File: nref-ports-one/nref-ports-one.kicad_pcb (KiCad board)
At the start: 2 copper layers, 84.9 x 17.5 mm, 4 parts, among them J3 USB_C_Receptacle

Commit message: ports-one WIP
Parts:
- removed REF**: WURTH_692121230100, footprints:WURTH_692121230100
- added C1: 1nF, Capacitor_SMD:C_0603_1608Metric, F.Cu at (137.7, 98.8)
- added C10: 0.1uF, Capacitor_SMD:C_0402_1005Metric, F.Cu at (103.6, 145.8)
- added C11: 10uF, Capacitor_SMD:C_0603_1608Metric, F.Cu at (102.2, 147.3)
- added C12: 10uF, Capacitor_SMD:C_0603_1608Metric, F.Cu at (102.2, 149.9)
- added C13: 0.1uF, Capacitor_SMD:C_0402_1005Metric, F.Cu at (111.6, 125.3)
- added C14: 0.1uF, Capacitor_SMD:C_0402_1005Metric, F.Cu at (109.1, 120.2)
- added C15: 0.1uF, Capacitor_SMD:C_0402_1005Metric, F.Cu at (109.1, 122.2)
- added C16: 10uF, Capacitor_SMD:C_0603_1608Metric, F.Cu at (106.2, 150.9)
- added C17: 47uF, Capacitor_SMD:C_1206_3216Metric, F.Cu at (118.6, 112.5)
- added C18: 0.1uF, Capacitor_SMD:C_0402_1005Metric, F.Cu at (117.1, 116.7)
- added C19: 22uF, Capacitor_SMD:C_0805_2012Metric, F.Cu at (104.1, 136.8)
- added C2: 0.1uF, Capacitor_SMD:C_0402_1005Metric, F.Cu at (137.7, 104.8)
- added C20: 22uF, Capacitor_SMD:C_0805_2012Metric, F.Cu at (104.2, 134.1)
- added C21: 47uF, Capacitor_SMD:C_1206_3216Metric, F.Cu at (118.5, 107.0)
- added C22: DNP, Capacitor_SMD:C_0402_1005Metric, F.Cu at (95.6, 149.1)
- added C23: 0.1uF, Capacitor_SMD:C_0402_1005Metric, F.Cu at (91.6, 127.1)
- added C24: 0.1uF, Capacitor_SMD:C_0402_1005Metric, F.Cu at (94.4, 115.3)
- added C25: 470nF, Capacitor_SMD:C_0603_1608Metric, F.Cu at (93.7, 122.9)
- added C26: 0.1uF, Capacitor_SMD:C_0402_1005Metric, F.Cu at (136.4, 123.3)
- added C27: 0.1uF, Capacitor_SMD:C_0402_1005Metric, F.Cu at (138.4, 121.2)
- added C28: 0.1uF, Capacitor_SMD:C_0402_1005Metric, F.Cu at (138.4, 123.2)
- added C29: 0.1uF, Capacitor_SMD:C_0402_1005Metric, F.Cu at (138.4, 125.2)
- added C3: 0.1uF, Capacitor_SMD:C_0402_1005Metric, F.Cu at (137.7, 106.8)
- added C30: 10uF, Capacitor_SMD:C_0603_1608Metric, F.Cu at (110.2, 140.8)
- added C31: 0.1uF, Capacitor_SMD:C_0402_1005Metric, F.Cu at (139.9, 123.1)
- added C32: 0.1uF, Capacitor_SMD:C_0402_1005Metric, F.Cu at (185.4, 128.1)
- added C33: 0.1uF, Capacitor_SMD:C_0402_1005Metric, F.Cu at (173.8, 112.2)
- added C34: 0.1uF, Capacitor_SMD:C_0402_1005Metric, F.Cu at (175.8, 112.2)
- added C35: 0.1uF, Capacitor_SMD:C_0402_1005Metric, F.Cu at (177.7, 112.2)
- added C36: 0.1uF, Capacitor_SMD:C_0402_1005Metric, F.Cu at (179.7, 112.2)
- added C37: 0.1uF, Capacitor_SMD:C_0402_1005Metric, F.Cu at (189.3, 135.7)
- added C4: 0.1uF, Capacitor_SMD:C_0402_1005Metric, F.Cu at (137.7, 108.7)
- added C5: 0.1uF, Capacitor_SMD:C_0402_1005Metric, F.Cu at (137.7, 110.7)
- added C6: 10uF, Capacitor_SMD:C_0603_1608Metric, F.Cu at (106.2, 143.3)
- added C7: 0.1uF, Capacitor_SMD:C_0402_1005Metric, F.Cu at (99.7, 131.7)
- added C8: 0.1uF, Capacitor_SMD:C_0402_1005Metric, F.Cu at (119.7, 117.6)
- added C9: 0.1uF, Capacitor_SMD:C_0402_1005Metric, F.Cu at (97.7, 134.6)
- added D1: LED_Small, LED_SMD:LED_0603_1608Metric, F.Cu at (167.2, 103.4)
- added D2: LED_Small, LED_SMD:LED_0603_1608Metric, F.Cu at (169.3, 103.4)
- added D3: SS54, Diode_SMD:D_SMA, F.Cu at (184.6, 138.7)
- added D4: PMEG4050EP,115, Diode_SMD:D_SOD-128, F.Cu at (183.6, 144.3)
- added FB1: 100@100MHz 3A, Inductor_SMD:L_0603_1608Metric, F.Cu at (96.2, 144.3)
- added FB10: 100@100MHz 3A, Inductor_SMD:L_0603_1608Metric, F.Cu at (122.9, 122.8)
- added FB2: DNP, Inductor_SMD:L_0603_1608Metric, F.Cu at (110.2, 145.8)
- added FB3: 100@100MHz 3A, Inductor_SMD:L_0603_1608Metric, F.Cu at (110.2, 148.4)
- added FB4: 100@100MHz 3A, Inductor_SMD:L_0603_1608Metric, F.Cu at (110.2, 150.9)
- added FB5: 100@100MHz 3A, Inductor_SMD:L_0603_1608Metric, F.Cu at (96.2, 146.4)
- added FB6: 100@100MHz 3A, Inductor_SMD:L_0603_1608Metric, F.Cu at (97.2, 140.3)
- added FB7: 100@100MHz 3A, Inductor_SMD:L_0603_1608Metric, F.Cu at (118.2, 123.3)
- added FB8: 100@100MHz 3A, Inductor_SMD:L_0603_1608Metric, F.Cu at (106.8, 128.7)
- added FB9: 100@100MHz 3A, Inductor_SMD:L_0603_1608Metric, F.Cu at (102.3, 125.1)
- added J1: CONN_HEAD, footprints:CUI_SJ-43614-SMT, F.Cu at (111.8, 108.0)
- added J10: CONN_SPK, Connector_Molex:Molex_PicoBlade_53261-0271_1x02-1MP_P1.25mm_Horizontal, F.Cu at (104.0, 117.0)
- added J2: DM3AT-SF-PEJM5, Connector_Card:microSD_HC_Hirose_DM3AT-SF-PEJM5, F.Cu at (129.2, 110.3)
- added J3: 09452812561, footprints:09452812561, F.Cu at (159.3, 110.2)
- added J5: Conn_01x10_Pin, Connector_FFC-FPC:Hirose_FH12-10S-0.5SH_1x10-1MP_P0.50mm_Horizontal, F.Cu at (117.7, 131.1)
- added J6: Conn_01x14_Pin, Connector_FFC-FPC:Hirose_FH12-14S-0.5SH_1x14-1MP_P0.50mm_Horizontal, F.Cu at (142.0, 131.0)
- added J7: Conn_01x12_Pin, Connector_FFC-FPC:Hirose_FH12-12S-0.5SH_1x12-1MP_P0.50mm_Horizontal, F.Cu at (154.8, 131.0)
- added J8: PWR, Connector_JST:JST_SH_SM09B-SRSS-TB_1x09-1MP_P1.00mm_Horizontal, F.Cu at (176.6, 129.9)
- added J9: Conn_01x10_Pin, Connector_FFC-FPC:Hirose_FH12-10S-0.5SH_1x10-1MP_P0.50mm_Horizontal, F.Cu at (129.6, 131.0)
- added L1: 15uH, Inductor_SMD:L_Taiyo-Yuden_NR-30xx, F.Cu at (102.3, 122.1)
- added L2: 15uH, Inductor_SMD:L_Taiyo-Yuden_NR-30xx, F.Cu at (106.9, 125.6)
- added R1: 1k, Resistor_SMD:R_0402_1005Metric, F.Cu at (167.0, 105.8)
- added R10: 33, Resistor_SMD:R_0402_1005Metric, F.Cu at (116.2, 126.9)
- added R11: 33, Resistor_SMD:R_0402_1005Metric, F.Cu at (115.2, 126.9)
- added R12: 100k, Resistor_SMD:R_0402_1005Metric, F.Cu at (107.1, 133.5)
- added R13: 2.2k, Resistor_SMD:R_0402_1005Metric, F.Cu at (108.1, 137.0)
- added R14: 10k, Resistor_SMD:R_0402_1005Metric, F.Cu at (133.5, 126.6)
- added R15: 0, Resistor_SMD:R_0402_1005Metric, F.Cu at (134.0, 124.5)
- added R16: 100k, Resistor_SMD:R_0402_1005Metric, F.Cu at (121.0, 127.0)
- added R17: 0, Resistor_SMD:R_0402_1005Metric, F.Cu at (184.5, 122.0)
- added R18: 0, Resistor_SMD:R_0402_1005Metric, F.Cu at (186.0, 124.5)
- added R19: 10k, Resistor_SMD:R_0402_1005Metric, F.Cu at (194.5, 140.5)
- added R2: 1k, Resistor_SMD:R_0402_1005Metric, F.Cu at (169.5, 105.8)
- added R3: 75 1%, Resistor_SMD:R_0402_1005Metric, F.Cu at (151.7, 104.5)
- added R4: 75 1%, Resistor_SMD:R_0402_1005Metric, F.Cu at (151.7, 106.5)
- added R5: 75 1%, Resistor_SMD:R_0402_1005Metric, F.Cu at (151.7, 108.5)
- added R6: 75 1%, Resistor_SMD:R_0402_1005Metric, F.Cu at (151.7, 110.5)
- added R7: 33, Resistor_SMD:R_0402_1005Metric, F.Cu at (117.2, 126.9)
- added R8: 33, Resistor_SMD:R_0402_1005Metric, F.Cu at (119.1, 126.9)
- added R9: 33, Resistor_SMD:R_0402_1005Metric, F.Cu at (118.1, 126.9)
- added TR1: TG111-MSC13LF, Transformer_SMD:Transformer_Ethernet_HALO_TG111-MSC13, F.Cu at (144.8, 109.4)
- added U1: TPS7A0533PDBZ, Package_TO_SOT_SMD:SOT-23, F.Cu at (119.0, 120.5)
- added U2: TLV320AIC3100, Package_DFN_QFN:VQFN-32-1EP_5x5mm_P0.5mm_EP3.5x3.5mm, F.Cu at (113.2, 120.4)
- added U3: TXS0108EPW, Package_SO:TSSOP-20_4.4x6.5mm_P0.65mm, F.Cu at (129.3, 123.5)
- added U4: SN74AVC1T45, Package_TO_SOT_SMD:SOT-23-6, F.Cu at (135.1, 121.6)
- added U5: TPD4E02B04DQA, Package_SON:USON-10_2.5x1.0mm_P0.5mm, F.Cu at (172.9, 114.7)
- added U6: TPD4E02B04DQA, Package_SON:USON-10_2.5x1.0mm_P0.5mm, F.Cu at (180.1, 114.9)
- added U7: TPD4E02B04DQA, Package_SON:USON-10_2.5x1.0mm_P0.5mm, F.Cu at (176.6, 115.0)
- added U8: FUSB302BMPX, Package_DFN_QFN:WQFN-14-1EP_2.5x2.5mm_P0.5mm_EP1.45x1.45mm, F.Cu at (184.6, 117.0)
- added U9: AP22815A, Package_TO_SOT_SMD:SOT-23-5, F.Cu at (190.6, 139.7)
- moved J4 17.4 mm to (176.6, 105.7)
- moved H2 11.0 mm to (184.8, 110.0)
- moved H1 10.00 mm to (103.8, 110.0)
- renumbered J3 to J4
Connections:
- J4 pad A1: (no net) -> GND
- J4 pad A10: (no net) -> USBH_2B_RXN
- J4 pad A11: (no net) -> USBH_2B_RXP
- J4 pad A12: (no net) -> GND
- J4 pad A2: (no net) -> /USBH_2A_AC_TXP
- J4 pad A3: (no net) -> /USBH_2A_AC_TXN
- J4 pad A4: (no net) -> USB_VBUS
- J4 pad A5: (no net) -> Net-(J4-CC1)
- J4 pad A6: (no net) -> USBH_2_DP
- J4 pad A7: (no net) -> USBH_2_DN
- J4 pad A8: (no net) -> unconnected-(J4-SBU1-PadA8)
- J4 pad A9: (no net) -> USB_VBUS
- J4 pad B1: (no net) -> GND
- J4 pad B10: (no net) -> USBH_2A_RXN
- J4 pad B11: (no net) -> USBH_2A_RXP
- J4 pad B12: (no net) -> GND
- J4 pad B2: (no net) -> /USBH_2B_AC_TXP
- J4 pad B3: (no net) -> /USBH_2B_AC_TXN
- J4 pad B4: (no net) -> USB_VBUS
- J4 pad B5: (no net) -> Net-(J4-CC2)
- J4 pad B6: (no net) -> USBH_2_DP
- J4 pad B7: (no net) -> USBH_2_DN
- J4 pad B8: (no net) -> unconnected-(J4-SBU2-PadB8)
- J4 pad B9: (no net) -> USB_VBUS
- J4 pad S1: (no net) -> GND
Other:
- board size 84.9 x 17.5 mm -> 88 x 27.9 mm

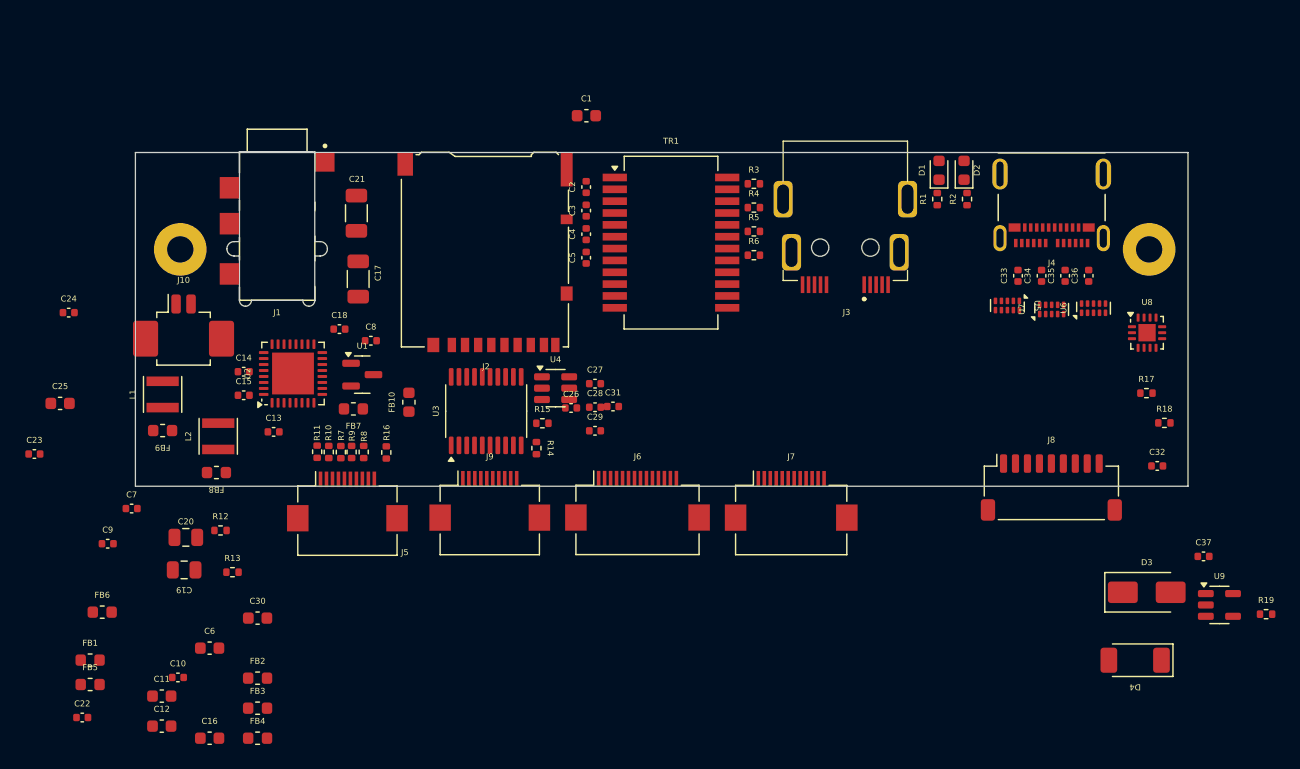
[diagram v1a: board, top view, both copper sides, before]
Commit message: ports one: some routing
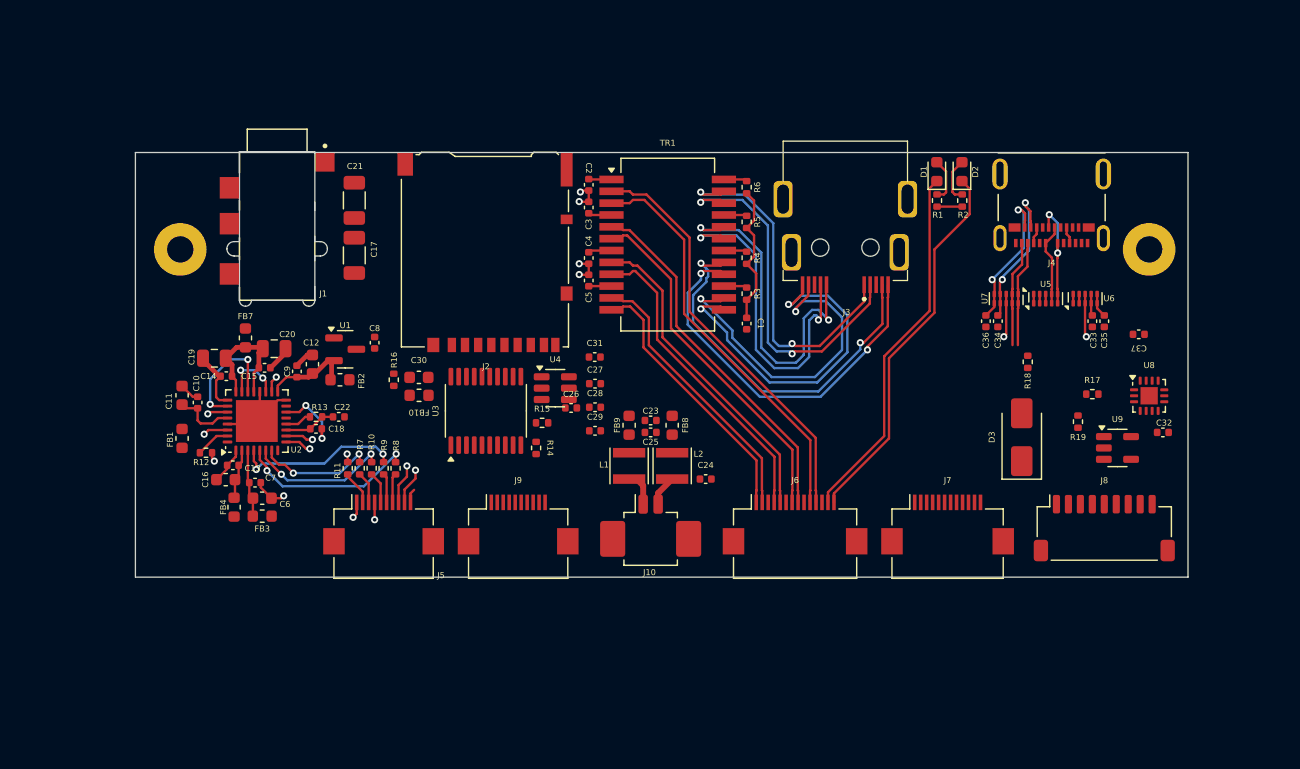
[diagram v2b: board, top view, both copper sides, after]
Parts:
- removed D4: PMEG4050EP,115, Diode_SMD:D_SOD-128
- removed FB5, FB6: 100@100MHz 3A, Inductor_SMD:L_0603_1608Metric
- C1, C25: footprint Capacitor_SMD:C_0603_1608Metric -> Capacitor_SMD:C_0402_1005Metric
- moved C24 55.0 mm to (147.7, 129.2)
- moved C23 51.6 mm to (143.1, 124.3)
- moved C25 49.4 mm to (143.1, 125.3)
- moved J10 42.5 mm to (143.1, 133.7)
- moved L1 39.5 mm to (141.3, 128.1), turned to -90 degrees
- moved FB9 39.0 mm to (141.3, 124.7), turned to -90 degrees
- moved FB8 38.3 mm to (144.9, 124.7), turned to -90 degrees
- moved L2 38.0 mm to (144.9, 128.1), turned to -90 degrees
- moved C22 33.0 mm to (117.0, 124.0), turned to 180 degrees
- moved C12 32.8 mm to (114.8, 119.6), turned to 90 degrees
- moved FB2 25.9 mm to (117.1, 120.9)
- moved C11 25.2 mm to (103.9, 122.2), turned to 90 degrees
- moved C30 24.2 mm to (123.7, 120.7)
- moved C10 23.0 mm to (105.2, 122.8), turned to 90 degrees
- moved R19 22.5 mm to (178.8, 124.4), turned to -90 degrees
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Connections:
- C24 pad 1: GNDA -> Net-(J10-Pin_2)
- C25 pad 2: GNDA -> Net-(J10-Pin_2)
- J10 pad 2: GNDA -> Net-(J10-Pin_2)
- J8 pad 1: GND -> VCC
- J8 pad 2: GND -> VCC
- L2 pad 2: GNDA -> Net-(J10-Pin_2)
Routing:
- net ETH0_A+: track 0.00 -> 34.6 mm
- net ETH0_A-: track 0.00 -> 33.9 mm
- net ETH0_DC-: track 0.00 -> 32.2 mm, vias 0 -> 2
- net ETH0_DC+: track 0.00 -> 32.0 mm, vias 0 -> 2
- net ETH0_LED_LINK1: track 0.00 -> 31.8 mm
- net ETH0_DA-: track 0.00 -> 30.7 mm, vias 0 -> 2
- net ETH0_LED_RX: track 0.00 -> 30.6 mm
- net ETH0_B+: track 0.00 -> 30.2 mm
- net ETH0_DA+: track 0.00 -> 30.0 mm, vias 0 -> 2
- net ETH0_DD-: track 0.00 -> 29.7 mm, vias 0 -> 2
- net ETH0_B-: track 0.00 -> 29.5 mm
- net ETH0_DB+: track 0.00 -> 29.2 mm, vias 0 -> 2
- net ETH0_DD+: track 0.00 -> 28.3 mm, vias 0 -> 2
- net ETH0_DB-: track 0.00 -> 28.2 mm, vias 0 -> 2
- net ETH0_C+: track 0.00 -> 27.0 mm
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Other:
- board size 88 x 27.9 mm -> 88 x 35.5 mm

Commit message: ports 1 routing, ports 2 location tweaks
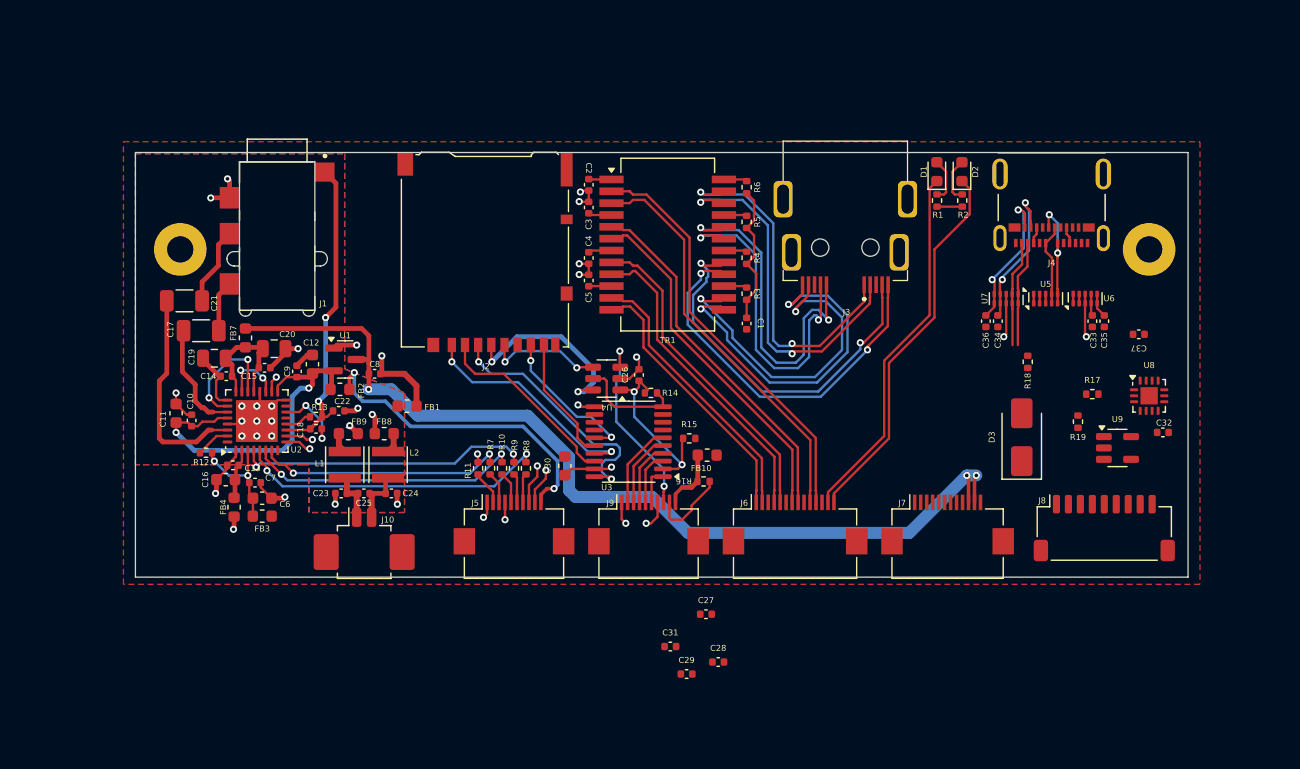
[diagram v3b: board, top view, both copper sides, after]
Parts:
- moved R16 27.3 mm to (147.5, 129.4), turned to 0 degrees
- moved C23 26.6 mm to (117.2, 130.4), turned to 180 degrees
- moved C24 26.3 mm to (121.4, 130.4)
- moved C31 25.0 mm to (144.7, 143.2)
- moved FB10 24.6 mm to (147.8, 127.2), turned to 0 degrees
- moved C25 24.5 mm to (119.1, 130.4)
- moved FB8 24.1 mm to (120.8, 125.4), turned to 0 degrees
- moved J10 24.0 mm to (119.1, 134.8)
- moved L1 23.8 mm to (117.5, 128.0)
- moved L2 23.8 mm to (121.1, 128.0)
- moved C28 23.7 mm to (148.7, 144.5)
- moved FB9 23.5 mm to (117.8, 125.4), turned to 180 degrees
- moved C29 21.7 mm to (146.1, 145.5)
- moved C27 21.4 mm to (147.7, 140.5)
- moved FB1 19.0 mm to (122.7, 123.1), turned to 180 degrees
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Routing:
- net +5V: track 0.00 -> 80.4 mm, vias 0 -> 3
- net +3V3: track 3.28 -> 66.4 mm, vias 0 -> 3
- net DAC_SDA: track 5.29 -> 36.0 mm
- net DAC_SCL: track 5.66 -> 35.5 mm
- net GND: track 23.2 -> 52.1 mm, vias 10 -> 17
- net SDC_CMD: track 0.00 -> 21.9 mm, vias 0 -> 2
- net HEAD_MIC: track 4.38 -> 26.2 mm, vias 0 -> 2
- net Net-(J2-VDD): track 0.00 -> 20.2 mm, vias 0 -> 3
- net SDC_D2: track 0.00 -> 19.3 mm, vias 0 -> 2
- net Net-(FB8-Pad1): track 5.21 -> 24.4 mm, vias 2 -> 3
- net /AUD_3V3: track 13.0 -> 30.3 mm, vias 0 -> 2
- net SDC_D3: track 0.00 -> 16.1 mm
- net Net-(U2-HPR): track 2.09 -> 18.0 mm, vias 1 -> 0
- net SD_CLK: track 0.00 -> 15.8 mm, vias 0 -> 2
- net Net-(U3-VCCA): track 0.00 -> 15.4 mm, vias 0 -> 2
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- added copper zone on F.Cu, net GND
- added copper zone on B.Cu, net GNDA
- added copper zone on F.Cu, net GNDA
- added copper zone on In1.Cu, net GNDA
- added copper zone on In2.Cu, net GNDA
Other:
- copper layers 2 -> 4

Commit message: ports one: more design and more routing
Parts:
- added C38: 47uF, Capacitor_SMD:C_1206_3216Metric, F.Cu at (167.8, 119.8)
- added C39: 47uF, Capacitor_SMD:C_1206_3216Metric, F.Cu at (169.9, 112.4)
- added C40: 47uF, Capacitor_SMD:C_1206_3216Metric, F.Cu at (167.6, 112.4)
- added C41: 0.1uF, Capacitor_SMD:C_0402_1005Metric, F.Cu at (162.0, 122.8)
- added C42: 0.1uF, Capacitor_SMD:C_0402_1005Metric, F.Cu at (176.6, 123.0)
- added C43: 1uF, Capacitor_SMD:C_0402_1005Metric, F.Cu at (107.0, 134.5)
- added C44: 1uF, Capacitor_SMD:C_0402_1005Metric, F.Cu at (112.2, 134.1)
- added R20: 0, Resistor_SMD:R_0402_1005Metric, F.Cu at (183.8, 116.0)
- added R21: 0, Resistor_SMD:R_0402_1005Metric, F.Cu at (185.8, 116.0)
- added R22: 0, Resistor_SMD:R_0402_1005Metric, F.Cu at (178.6, 121.7)
- added R23: 200k, Resistor_SMD:R_0402_1005Metric, F.Cu at (176.6, 121.7)
- added R24: 0, Resistor_SMD:R_0402_1005Metric, F.Cu at (166.6, 122.7)
- added R25: 200k, Resistor_SMD:R_0402_1005Metric, F.Cu at (165.1, 120.1)
- added R26: 200k, Resistor_SMD:R_0402_1005Metric, F.Cu at (164.1, 120.1)
- added R27: 200k, Resistor_SMD:R_0402_1005Metric, F.Cu at (167.6, 116.9)
- added R28: 10k, Resistor_SMD:R_0402_1005Metric, F.Cu at (166.1, 120.1)
- added R29: 900k, Resistor_SMD:R_0402_1005Metric, F.Cu at (167.2, 124.5)
- added R30: 200k, Resistor_SMD:R_0402_1005Metric, F.Cu at (165.7, 124.2)
- added R31: 0, Resistor_SMD:R_0402_1005Metric, F.Cu at (177.9, 120.6)
- added R32: 0, Resistor_SMD:R_0402_1005Metric, F.Cu at (184.7, 130.2)
- added R33: 0, Resistor_SMD:R_0402_1005Metric, F.Cu at (184.7, 129.2)
- added R34: 10k, Resistor_SMD:R_0402_1005Metric, F.Cu at (160.5, 122.8)
- added U10: HD3SS3220IRNHT, footprints:QFN40P450X250X80-31N120X320, F.Cu at (172.8, 120.4)
- added U11: PCAL6416AHF, Package_DFN_QFN:HVQFN-24-1EP_4x4mm_P0.5mm_EP2.1x2.1mm, F.Cu at (162.2, 126.6)
- added U12: TLV75518PDBV, Package_TO_SOT_SMD:SOT-23-5, F.Cu at (109.6, 134.8)
- moved C31 27.0 mm to (129.6, 120.8), turned to -90 degrees
- moved C29 25.9 mm to (136.7, 121.4), turned to -90 degrees
- moved C28 20.9 mm to (136.0, 127.9), turned to 90 degrees
- moved C27 13.8 mm to (146.2, 126.8)
- moved C32 12.5 mm to (173.6, 127.6), turned to -90 degrees
- moved R18 10.8 mm to (184.8, 116.0)
- moved C37 10.6 mm to (182.4, 127.6), turned to 90 degrees
- moved C30 8.32 mm to (130.9, 121.5), turned to -90 degrees
- moved R17 6.71 mm to (182.8, 116.0), turned to -90 degrees
- moved U9 6.31 mm to (175.8, 127.5), turned to 90 degrees
- moved D3 5.47 mm to (179.3, 127.2)
- moved U8 2.78 mm to (183.6, 124.8)
- moved R19 2.29 mm to (176.6, 124.8), turned to 180 degrees
- moved R14 1.05 mm to (144.2, 122.0)
- moved J8 0.96 mm to (180.8, 134.2)
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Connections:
- net Net-(J4-CC1) renamed CC1
- net Net-(J4-CC2) renamed CC2
- D3 pad 1: VCHG -> VPD
- J4 pad A6: USBH_2_DP -> USB1_DP
- J4 pad A7: USBH_2_DN -> USB1_DN
- J4 pad B6: USBH_2_DP -> USB1_DP
- J4 pad B7: USBH_2_DN -> USB1_DN
- U5 pad 4: USBH_2_DN -> USB1_DN
- U5 pad 5: USBH_2_DP -> USB1_DP
- U5 pad 6: USBH_2_DP -> USB1_DP
- U5 pad 7: USBH_2_DN -> USB1_DN
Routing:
- net +1V8: track 0.00 -> 50.4 mm, vias 0 -> 2
- net RP_SCL0: track 0.00 -> 48.0 mm, vias 0 -> 3
- net RP_SDA0: track 0.00 -> 43.9 mm, vias 0 -> 2
- net GND: track 52.1 -> 95.6 mm, vias 17 -> 34
- net USB1_DP: track 0.00 -> 32.3 mm, vias 0 -> 4
- net USB1_DN: track 0.00 -> 29.2 mm, vias 0 -> 2
- net CC2: track 0.77 -> 22.1 mm, vias 0 -> 3
- net USBH_2A_RXN: track 0.77 -> 20.0 mm, vias 0 -> 4
- net CC1: track 0.77 -> 19.4 mm, vias 0 -> 3
- net USB1_TXN: track 0.00 -> 18.1 mm, vias 0 -> 2
- net USBH_2A_RXP: track 0.77 -> 18.4 mm, vias 0 -> 4
- net USB1_TXP: track 0.00 -> 17.4 mm, vias 0 -> 2
- net USB1_RXN: track 0.00 -> 16.4 mm, vias 0 -> 2
- net USB_VBUS: track 2.81 -> 19.1 mm, vias 0 -> 2
- net STANDBY_3V3: track 0.00 -> 16.0 mm
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
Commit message: ports-one snapshot
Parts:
- added H3: BADGE, footprints:nref-ports-one-badge, B.Cu at (131.1, 109.2)
- added R35: 0, Resistor_SMD:R_0402_1005Metric, F.Cu at (166.9, 116.5)
- H1: value MountingHole_2.2mm_M2_Pad -> MountingHole; footprint MountingHole:MountingHole_2.2mm_M2_Pad -> MountingHole:MountingHole_2.2mm_M2
- H2: value MountingHole_2.2mm_M2_Pad -> MountingHole_Pad
- moved R33 22.2 mm to (164.0, 121.3)
- moved R32 21.4 mm to (164.8, 122.4)
- moved R25 1.50 mm to (165.1, 118.6)
- moved R28 1.50 mm to (166.1, 118.6)
- moved R27 1.41 mm to (168.9, 116.5)
- moved R26 0.50 mm to (164.1, 119.6)
- moved R24 0.40 mm to (167.0, 122.6)
- moved R1 0.28 mm to (167.0, 106.2)
- moved R2 0.28 mm to (169.1, 106.2)
- moved C42 0.25 mm to (176.3, 123.0)
- moved D1 0.20 mm to (167.0, 103.7)
- moved D2 0.20 mm to (169.1, 103.7)
- moved C38 0.15 mm to (167.9, 119.8)
- moved FB10 0.11 mm to (148.2, 128.1)
- moved FB7 0.10 mm to (109.1, 117.4)
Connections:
- H2 pad 1: (no net) -> GND
- J2 pad 10: (no net) -> GND
- J2 pad 11: (no net) -> GND
- J2 pad 9: (no net) -> SD_DET
- U10 pad 29: GND -> Net-(U10-~{ENN_CC})
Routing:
- net +3V3: track 72.1 -> 156.6 mm, vias 4 -> 6
- net USB_VBUS: track 19.1 -> 94.6 mm, vias 2 -> 10
- net Net-(U10-CC2): track 1.99 -> 66.3 mm, vias 1 -> 3
- net Net-(U10-CC1): track 3.34 -> 65.8 mm, vias 1 -> 3
- net RP_FUSB_INT: track 3.06 -> 46.3 mm
- net STANDBY_3V3: track 16.0 -> 53.0 mm, vias 0 -> 2
- net USB_SRC_EN: track 1.80 -> 32.5 mm, vias 2 -> 4
- net SD_DET: track 6.57 -> 34.3 mm, vias 0 -> 2
- net GND: track 95.6 -> 119.0 mm, vias 34 -> 75
- net Net-(U2-MCLK): track 0.71 -> 20.8 mm, vias 1 -> 2
- net Net-(J2-VDD): track 25.7 -> 40.5 mm, vias 3 -> 2
- net Net-(U10-~{ENN_CC}): track 0.00 -> 12.4 mm, vias 0 -> 2
- net +5V: track 90.9 -> 99.7 mm, vias 4 -> 5
- net Net-(U10-SDA/OUT1): track 2.30 -> 9.27 mm
- net Net-(U10-SCL/OUT2): track 2.81 -> 7.66 mm
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- added copper zone on B.Cu, net GND
- added copper zone on In1.Cu, net GND
- added copper zone on In2.Cu, net GND
